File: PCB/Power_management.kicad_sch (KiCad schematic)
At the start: 75 parts, among them Q2 2N7002E, U2 TPS65400RGZR

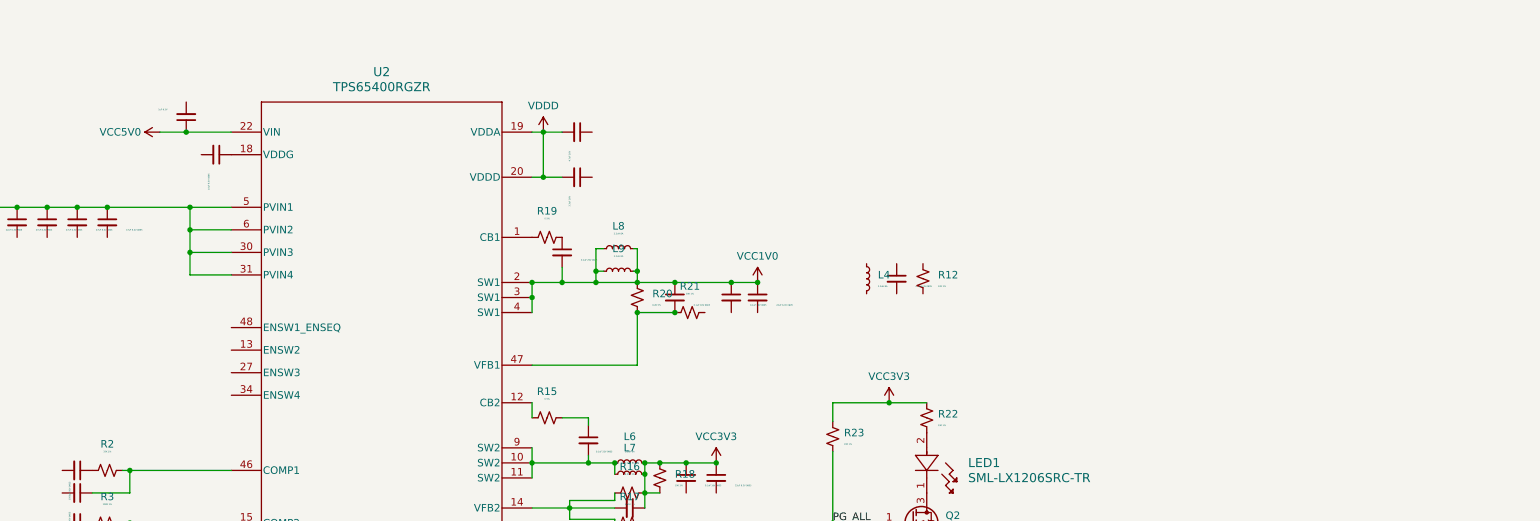
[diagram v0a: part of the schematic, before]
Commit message: [+] add fpga footprint
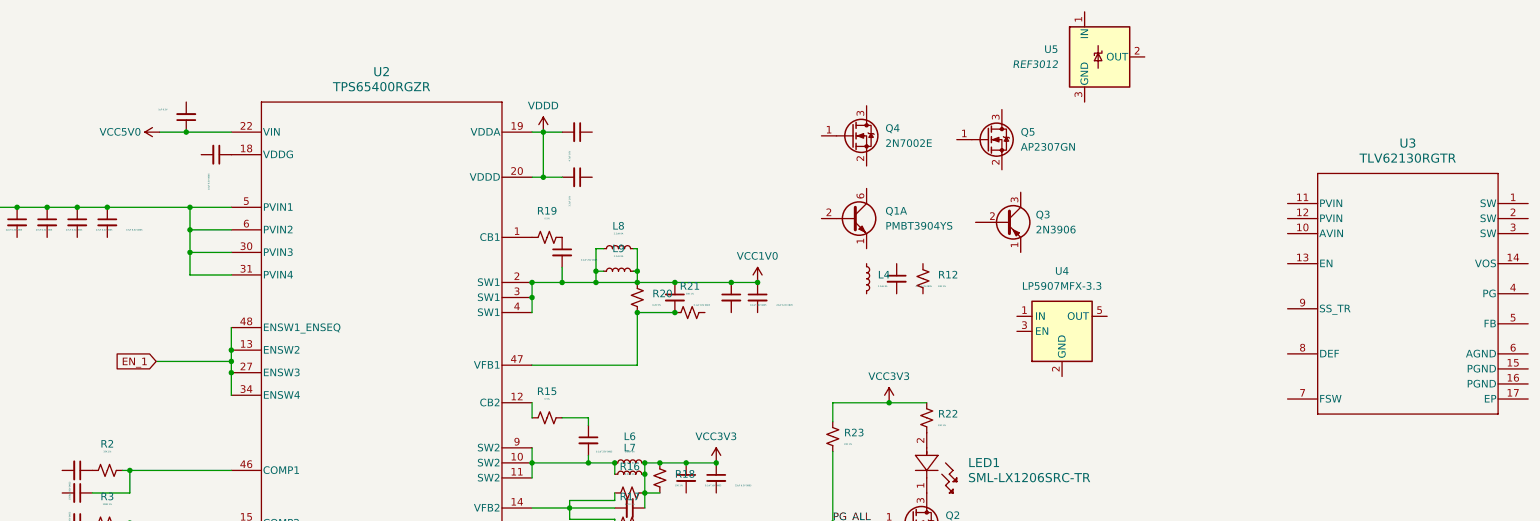
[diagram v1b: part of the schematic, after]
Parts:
- added Q1: PMBT3904YS, Package_TO_SOT_SMD:SOT-363_SC-70-6, symbol Transistor_BJT:PMBT3904YS
- added Q3: 2N3906, Package_TO_SOT_THT:TO-92_Inline, symbol Transistor_BJT:2N3906
- added Q4: 2N7002E, Package_TO_SOT_SMD:SOT-23, symbol Transistor_FET:2N7002E
- added Q5: AP2307GN, Package_TO_SOT_SMD:SOT-23, symbol Transistor_FET:2N7002E
- added U3: TLV62130RGTR, RGT0016C, symbol 2025-02-15_04-06-27:TLV62130RGTR
- added U4: LP5907MFX-3.3, Package_TO_SOT_SMD:SOT-23-5, symbol Regulator_Linear:LP5907MFX-3.3
- added U5: REF3012, Package_TO_SOT_SMD:SOT-23, symbol Reference_Voltage:REF3012
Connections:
- net EN_1: now reaches U2.13 (ENSW2)
- net EN_1: now also U2.27 (ENSW3), U2.34 (ENSW4), U2.48 (ENSW1_ENSEQ)

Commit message: [+] pushing to save major progress
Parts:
- removed C28: 47uF 6.3V 0805, symbol Device:C_Small
- removed L4: 2.2uH 8A, symbol Device:L_Small
- removed Q1: PMBT3904YS, Package_TO_SOT_SMD:SOT-363_SC-70-6, symbol Transistor_BJT:PMBT3904YS
- removed Q3: 2N3906, Package_TO_SOT_THT:TO-92_Inline, symbol Transistor_BJT:2N3906
- removed Q4: 2N7002E, Package_TO_SOT_SMD:SOT-23, symbol Transistor_FET:2N7002E
- removed Q5: AP2307GN, Package_TO_SOT_SMD:SOT-23, symbol Transistor_FET:2N7002E
- removed U4: LP5907MFX-3.3, Package_TO_SOT_SMD:SOT-23-5, symbol Regulator_Linear:LP5907MFX-3.3
- removed U5: REF3012, Package_TO_SOT_SMD:SOT-23, symbol Reference_Voltage:REF3012
- added C41, C45, C47: 0.1uF 16V 0805, symbol Device:C_Small
- added C42: 0.1uF16V 0805, symbol Device:C_Small
- added C43: 22uF 25V 0805, symbol Device:C_Small
- added C44: 3300pF 50V 0805, symbol Device:C_Small
- added C46: 22uF 6.3V, symbol Device:C_Small
- added C48, C49: 1uF 6.3V, symbol Device:C_Small
- added C50: 1uF6.3V, symbol Device:C_Small
- added C51, C52: 0.1uF16V, symbol Device:C_Small
- added FB1: 70 Ohm 100MHz 3A, Inductor_SMD:L_0603_1608Metric, symbol Device:FerriteBead_Small
- added J1: PJ-037AH, PJ-037AH:CUI_PJ-037AH, symbol PJ-037AH:PJ-037AH
- added L10: 2.2uH 3A, symbol Device:L_Small
- added Q10: AP2307GN, Package_TO_SOT_SMD:SOT-23, symbol Transistor_FET:2N7002E
- added Q11, Q9: 2N7002E, Package_TO_SOT_SMD:SOT-23, symbol Transistor_FET:2N7002E
- added Q6: PMBT3904YS, Package_TO_SOT_SMD:SOT-363_SC-70-6, symbol Transistor_BJT:PMBT3904YS
- added Q7, Q8: 2N3906, Package_TO_SOT_THT:TO-92_Inline, symbol Transistor_BJT:2N3906
- added R24, R25, R27, R32, R33, R34, R36, R37, R39: 10K 1%, symbol Device:R_Small_US
- added R26: 100k 1%, symbol Device:R_Small_US
- added R28, R29: 0 /X, symbol Device:R_Small_US
- added R30: 69.8K 1%, symbol Device:R_Small_US
- added R31: 13.3K 1%, symbol Device:R_Small_US
- added R35, R38: 20K 1%, symbol Device:R_Small_US
- added SW2: SW_Wuerth_450301014042, Button_Switch_SMD:SW_SPST_CK_KMS2xxGP, symbol Switch:SW_Wuerth_450301014042
- added U6: LP5907MFX-3.3, Package_TO_SOT_SMD:SOT-23-5, symbol Regulator_Linear:LP5907MFX-3.3
- added U7: REF3012, Package_TO_SOT_SMD:SOT-23, symbol Reference_Voltage:REF3012
- R12: value 33K 1% -> 10K 1%
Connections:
- net EN_1: now also Q11.3 (D), R38.1, R39.2
- net GND: now also C1.2, C10.1, C12.2, C13.2, C14.2, C15.2, C16.2, C17.2, C18.2, C19.2, C2.2, C20.2, C21.2, C22.2, C23.2, C26.2, C27.2, C3.2, C30.2, C31.2, C34.2, C35.2, C4.2, C5.2, C6.2, C7.2, C8.2, C9.1, R1.2, R10.1, R17.1, R23.2, R7.2, U2.21 (AGND), U2.49 (PAD), U2.7 (PGND1), U2.8 (PGND2), U3.8 (DEF), C41.2, C44.1, C48.2, C49.2, C50.2, C51.2, C52.2, J1.2, Q11.2 (S), Q6.1 (E1), Q9.2 (S), R27.2, R29.2, R31.2, R35.1, R39.1, SW2.2 (C), U6.2 (GND), U7.3 (GND)
- net VCC1V8: now also C50.1, FB1.2
- net VCC3V3: now also C40.1, Q2.1 (G), U2.17 (PGOOD); no longer R23.1
- net VCC5V0: now also U3.14 (VOS), C45.1, C46.1, C48.1, L10.1, R28.1, R30.1, R38.2, U6.1 (IN), U6.3 (EN)
- net at R21.2: now also C38.2, C39.2, R23.1
- net at U3.1 (SW): now also U3.2 (SW), U3.3 (SW), L10.2
- net VU: now reaches U3.10 (AVIN)
- net VU: now also R12.1, U3.11 (PVIN), U3.12 (PVIN), C42.1, C43.1, C47.1, J1.1, Q10.2 (S), Q7.3 (C), Q8.3 (C), R32.1, R36.2
- net EN_6213: now reaches U3.13 (EN)
- net at U3.15 (PGND): now also U3.16 (PGND), U3.17 (EP), U3.6 (AGND)
- net at U3.5 (FB): now also R30.2, R31.1
- net at U3.7 (FSW): now also R28.2, R29.1
- net at U3.9 (SS_TR): now also C44.2
- net at R12.2: now also Q6.6 (C1), R25.2
- removed net PG_ALL: C40.1, Q2.1 (G), R23.2, U2.17 (PGOOD)
- new net: Q11.1 (G), R32.2, R33.2, SW2.3 (A)
- new net: Q9.3 (D), R37.1
- new net: Q6.2 (B1), R24.1
- new net: Q7.1 (E), R26.1
- new net: C41.1, R26.2, R27.1
- new net: Q7.2 (B), R25.1
- new net: Q8.1 (E), R34.2
- new net: Q8.2 (B), R33.1
- new net: C47.2, Q10.1 (G), R36.1, R37.2
- new net AVCC3V3: C49.1, U6.5 (OUT)
- new net EN_MAIN: Q9.1 (G), R24.2, R34.1, R35.2
- new net VU_CK: Q10.3 (D)
- new net XADC1V8: C51.1, FB1.1, U7.1 (IN)
- new net XADCVREF: C52.1, U7.2 (OUT)
- no-connect marks 2 -> 3
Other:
- note added: "MUST CHECK THIS ONCE"
- moved on the sheet: L1, L2, L3, L5, L6, L7, L8, L9, LED1, Q2, R1, R10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

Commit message: some part done
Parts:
- C401: renamed from C4; footprint (none) -> Capacitor_SMD:C_0805_2012Metric
- C402: renamed from C5; footprint (none) -> Capacitor_SMD:C_0805_2012Metric
- C403: renamed from C6; footprint (none) -> Capacitor_SMD:C_0805_2012Metric
- C404: renamed from C2; footprint (none) -> Capacitor_SMD:C_0805_2012Metric
- C405: renamed from C1; footprint (none) -> Capacitor_SMD:C_0805_2012Metric
- C406: renamed from C12; footprint (none) -> Capacitor_SMD:C_0603_1608Metric
- C407: renamed from C13; footprint (none) -> Capacitor_SMD:C_0603_1608Metric
- C408: renamed from C14; footprint (none) -> Capacitor_SMD:C_0603_1608Metric
- C409: renamed from C15; footprint (none) -> Capacitor_SMD:C_0603_1608Metric
- C410: renamed from C16; footprint (none) -> Capacitor_SMD:C_0603_1608Metric
- C411: renamed from C17; footprint (none) -> Capacitor_SMD:C_0603_1608Metric
- C412: renamed from C18; footprint (none) -> Capacitor_SMD:C_0603_1608Metric
- C413: renamed from C19; footprint (none) -> Capacitor_SMD:C_0603_1608Metric
- C414: renamed from C3; footprint (none) -> Capacitor_SMD:C_0805_2012Metric
- C415: renamed from C20; footprint (none) -> Capacitor_SMD:C_0603_1608Metric
- C416: renamed from C21; footprint (none) -> Capacitor_SMD:C_0603_1608Metric
- C417: renamed from C22; footprint (none) -> Capacitor_SMD:C_0603_1608Metric
- C418: renamed from C23; footprint (none) -> Capacitor_SMD:C_0603_1608Metric
- C419: renamed from C8; footprint (none) -> Capacitor_SMD:C_0805_2012Metric
- C420: renamed from C7; footprint (none) -> Capacitor_SMD:C_0805_2012Metric
- C421: renamed from C36; footprint (none) -> Capacitor_SMD:C_0603_1608Metric
- C422: renamed from C9; footprint (none) -> Capacitor_SMD:C_0805_2012Metric
- C423: renamed from C10; footprint (none) -> Capacitor_SMD:C_0805_2012Metric
- C424: renamed from C11; footprint (none) -> Capacitor_SMD:C_0805_2012Metric
- C425: renamed from C32; footprint (none) -> Capacitor_SMD:C_0805_2012Metric
- C426: renamed from C25; footprint (none) -> Capacitor_SMD:C_0805_2012Metric
- C427: renamed from C29; footprint (none) -> Capacitor_SMD:C_0805_2012Metric
- C428: renamed from C33; footprint (none) -> Capacitor_SMD:C_0805_2012Metric
- C429: renamed from C24; footprint (none) -> Capacitor_SMD:C_0805_2012Metric
- C430: renamed from C37; footprint (none) -> Capacitor_SMD:C_0805_2012Metric
- C431: renamed from C30; footprint (none) -> Capacitor_SMD:C_0805_2012Metric
- C432: renamed from C34; footprint (none) -> Capacitor_SMD:C_0805_2012Metric
- C433: renamed from C26; footprint (none) -> Capacitor_SMD:C_0805_2012Metric
- C434: renamed from C31; footprint (none) -> Capacitor_SMD:C_0805_2012Metric
- C435: renamed from C35; footprint (none) -> Capacitor_SMD:C_0805_2012Metric
- C436: renamed from C27; footprint (none) -> Capacitor_SMD:C_0805_2012Metric
- C437: renamed from C38; footprint (none) -> Capacitor_SMD:C_0805_2012Metric
- C438: renamed from C39; footprint (none) -> Capacitor_SMD:C_0805_2012Metric
- C439: renamed from C40; footprint (none) -> Capacitor_SMD:C_0805_2012Metric
- C440: renamed from C42; footprint (none) -> Capacitor_SMD:C_0805_2012Metric
- C441: renamed from C43; footprint (none) -> Capacitor_SMD:C_0805_2012Metric
- C442: renamed from C44; footprint (none) -> Capacitor_SMD:C_0805_2012Metric
- C443: renamed from C41; footprint (none) -> Capacitor_SMD:C_0805_2012Metric
- C444: renamed from C45; footprint (none) -> Capacitor_SMD:C_0805_2012Metric
- C445: renamed from C46; footprint (none) -> Capacitor_SMD:C_0805_2012Metric
- C446: renamed from C47; footprint (none) -> Capacitor_SMD:C_0805_2012Metric
- C447: renamed from C50; footprint (none) -> Capacitor_SMD:C_0805_2012Metric
- C448: renamed from C48; footprint (none) -> Capacitor_SMD:C_0805_2012Metric
- C449: renamed from C51; footprint (none) -> Capacitor_SMD:C_0805_2012Metric
- C450: renamed from C49; footprint (none) -> Capacitor_SMD:C_0805_2012Metric
- C451: renamed from C52; footprint (none) -> Capacitor_SMD:C_0805_2012Metric
- L401: renamed from L8; footprint (none) -> Inductor_SMD:L_1806_4516Metric
- L402: renamed from L9; footprint (none) -> Inductor_SMD:L_1806_4516Metric
- L403: renamed from L1; footprint (none) -> Inductor_SMD:L_1806_4516Metric
- L404: renamed from L5; footprint (none) -> Inductor_SMD:L_1806_4516Metric
- L405: renamed from L6; footprint (none) -> Inductor_SMD:L_1806_4516Metric
- L406: renamed from L7; footprint (none) -> Inductor_SMD:L_1806_4516Metric
- L407: renamed from L2; footprint (none) -> Inductor_SMD:L_1806_4516Metric
- L408: renamed from L3; footprint (none) -> Inductor_SMD:L_1806_4516Metric
- L409: renamed from L10; footprint (none) -> Inductor_SMD:L_1806_4516Metric
- LED401: renamed from LED1; footprint LED_3P2X1P5_LUM -> ul_SML-LX1206SRC-TR:LED_3P2X1P5_LUM
- R401: renamed from R2; footprint (none) -> Resistor_SMD:R_0805_2012Metric
- R402: renamed from R3; footprint (none) -> Resistor_SMD:R_0805_2012Metric
- R403: renamed from R4; footprint (none) -> Resistor_SMD:R_0805_2012Metric
- R404: renamed from R5; footprint (none) -> Resistor_SMD:R_0805_2012Metric
- R405: renamed from R1; footprint (none) -> Resistor_SMD:R_0805_2012Metric
- R406: renamed from R7; footprint (none) -> Resistor_SMD:R_0805_2012Metric
- R407: renamed from R8; footprint (none) -> Resistor_SMD:R_0805_2012Metric
- R408: renamed from R6; footprint (none) -> Resistor_SMD:R_0805_2012Metric
- R409: renamed from R19; footprint (none) -> Resistor_SMD:R_0805_2012Metric
- R410: renamed from R15; footprint (none) -> Resistor_SMD:R_0805_2012Metric
- R411: renamed from R11; footprint (none) -> Resistor_SMD:R_0805_2012Metric
- R412: renamed from R13; footprint (none) -> Resistor_SMD:R_0805_2012Metric
- R413: renamed from R14; footprint (none) -> Resistor_SMD:R_0805_2012Metric
- R414: renamed from R16; footprint (none) -> Resistor_SMD:R_0805_2012Metric
- R415: renamed from R17; footprint (none) -> Resistor_SMD:R_0805_2012Metric
- R416: renamed from R9; footprint (none) -> Resistor_SMD:R_0805_2012Metric
- R417: renamed from R10; footprint (none) -> Resistor_SMD:R_0805_2012Metric
- R418: renamed from R20; footprint (none) -> Resistor_SMD:R_0805_2012Metric
- R419: renamed from R18; footprint (none) -> Resistor_SMD:R_0805_2012Metric
- R420: renamed from R21; footprint (none) -> Resistor_SMD:R_0805_2012Metric
- R421: renamed from R23; footprint (none) -> Resistor_SMD:R_0805_2012Metric
- R422: renamed from R22; footprint (none) -> Resistor_SMD:R_0805_2012Metric
- R423: renamed from R28; footprint (none) -> Resistor_SMD:R_0805_2012Metric
- R424: renamed from R29; footprint (none) -> Resistor_SMD:R_0805_2012Metric
- R425: renamed from R24; footprint (none) -> Resistor_SMD:R_0805_2012Metric
- R426: renamed from R12; footprint (none) -> Resistor_SMD:R_0805_2012Metric
- R427: renamed from R25; footprint (none) -> Resistor_SMD:R_0805_2012Metric
- R428: renamed from R26; footprint (none) -> Resistor_SMD:R_0805_2012Metric
- R429: renamed from R27; footprint (none) -> Resistor_SMD:R_0805_2012Metric
- R430: renamed from R30; footprint (none) -> Resistor_SMD:R_0805_2012Metric
- R431: renamed from R31; footprint (none) -> Resistor_SMD:R_0805_2012Metric
- R432: renamed from R36; footprint (none) -> Resistor_SMD:R_0805_2012Metric
- R433: renamed from R37; footprint (none) -> Resistor_SMD:R_0805_2012Metric
- R434: renamed from R32; footprint (none) -> Resistor_SMD:R_0805_2012Metric
- R435: renamed from R33; footprint (none) -> Resistor_SMD:R_0805_2012Metric
- R436: renamed from R38; footprint (none) -> Resistor_SMD:R_0805_2012Metric
- R437: renamed from R39; footprint (none) -> Resistor_SMD:R_0805_2012Metric
- R438: renamed from R34; footprint (none) -> Resistor_SMD:R_0805_2012Metric
- R439: renamed from R35; footprint (none) -> Resistor_SMD:R_0805_2012Metric
- U401: renamed from U2; footprint RGZ0048B -> TPS65400RGZR:RGZ0048B
- U402: renamed from U3; footprint RGT0016C -> footprints:RGT0016C
- renumbered FB1 to FB401, J1 to J401, Q2 to Q401, Q6 to Q402, Q7 to Q403, Q9 to Q404, Q11 to Q405, Q10 to Q406, Q8 to Q407, SW2 to SW401, U6 to U403, U7 to U404
